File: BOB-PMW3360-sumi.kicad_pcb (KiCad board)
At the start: 2 copper layers, 30 x 20 mm, 14 parts, among them J4 Conn_02x04_Odd_Even, U1 TLV70019_SOT23-5, U2 PMW3360DM-T2QU

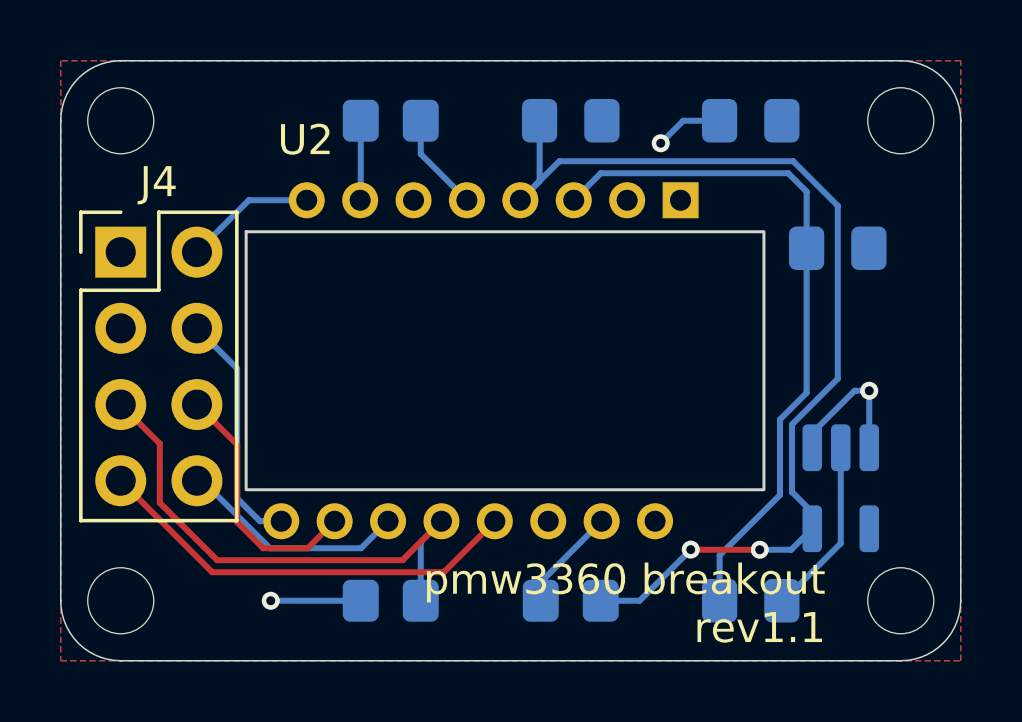
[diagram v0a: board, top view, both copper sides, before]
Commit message: シルクスクリーンとkicadのバージョンを8から9へ変更
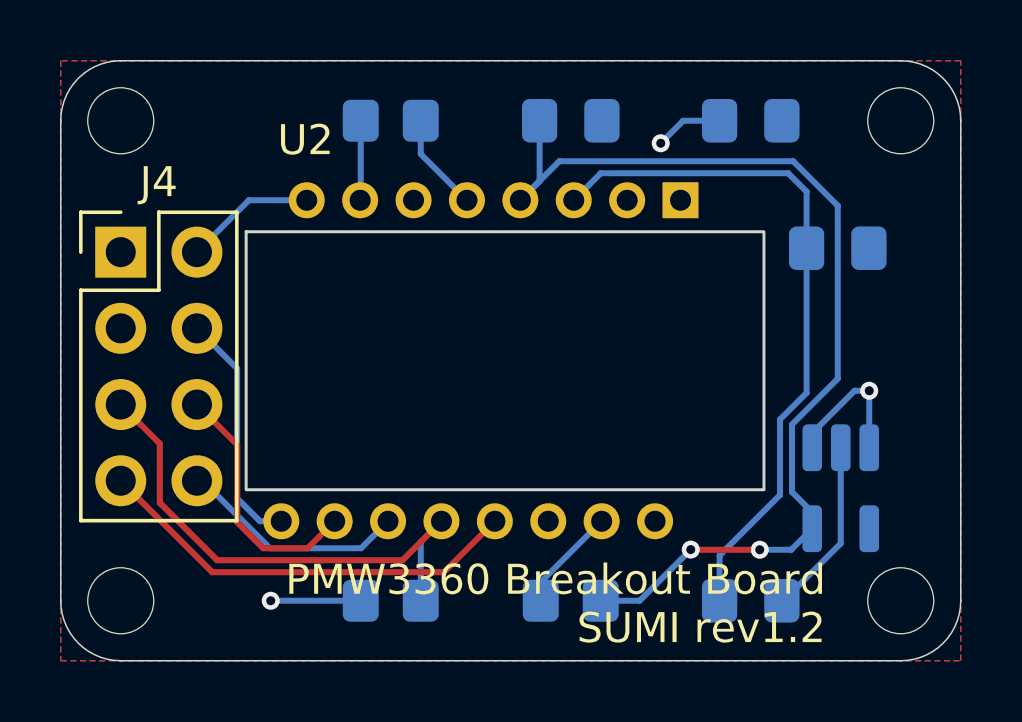
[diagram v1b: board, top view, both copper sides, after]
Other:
- board text added: "MOT"
- board text added: "PMW3360 Breakout Board SUMI rev1.2"
- board text removed: "MOTION"
- board text removed: "pmw3360 breakout rev1.1"
